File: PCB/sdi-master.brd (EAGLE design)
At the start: 71 x 18.2 mm, 21 parts, among them U1 ATSAMD11C14A-SSUT, U3 LDL1117S12R

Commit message: removed buttons.. not needed
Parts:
- removed R3: 2k, SparkFun-Resistors:1206
- removed S1: MOMENTARY-SWITCH-SPST-SMD-6.0X3.5MM, SparkFun-Switches:TACTILE_SWITCH_SMD_6.0X3.5MM
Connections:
- removed net N$1: R3.2, S1.1, U1.1
- net 3.3V: no longer S1.2
- net GND: no longer R3.1
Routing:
- net N$1: track 63.9 -> 0.00 mm, vias 2 -> 0
- net 3.3V: track 72.3 -> 60.1 mm
- net GND: vias 5 -> 1
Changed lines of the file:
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@@
 <?xml version="1.0" encoding="utf-8"?>
 <!DOCTYPE eagle SYSTEM "eagle.dtd">
-<eagle version="9.2.2">
+<eagle version="9.3.0">
 <drawing>
 <settings>
@@
 <attribute name="VALUE" x="31.67" y="14.032" size="0.6096" layer="27" font="vector" ratio="20" rot="R180"/>
 </element>
-<element name="S1" library="SparkFun-Switches" package="TACTILE_SWITCH_SMD_6.0X3.5MM" value="MOMENTARY-SWITCH-SPST-SMD-6.0X3.5MM" x="58.5" y="18.1" smashed="yes" rot="R270">
-<attribute name="NAME" x="60.405" y="18.1" size="0.6096" layer="25" font="vector" ratio="20" rot="R270" align="bottom-center"/>
-<attribute name="PROD_ID" value="SWCH-00815" x="58.5" y="18.1" size="1.778" layer="27" rot="R270" display="off"/>
-<attribute name="SF_SKU" value="COM-08229" x="58.5" y="18.1" size="1.778" layer="27" rot="R270" display="off"/>
-</element>
-<element name="R3" library="SparkFun-Resistors" package="1206" value="2k" x="54.6" y="13.1" smashed="yes">
-<attribute name="NAME" x="53.33" y="14.243" size="0.4064" layer="25"/>
-<attribute name="VALUE" x="53.203" y="11.576" size="0.4064" layer="27"/>
-</element>
 </elements>
 <signals>
@@
 <contactref element="J1" pad="SHIELD3"/>
 <contactref element="J2" pad="1"/>
-<contactref element="R3" pad="1"/>
-<via x="47.6" y="17.2" extent="1-16" drill="0.25"/>
-<via x="53.8" y="16.7" extent="1-16" drill="0.25"/>
-<via x="52.1" y="14.9" extent="1-16" drill="0.25"/>
-<via x="47.2" y="14.9" extent="1-16" drill="0.25"/>
 <wire x1="37.69" y1="12.847" x2="36.937" y2="13.6" width="0.254" layer="1"/>
 <wire x1="36.937" y1="13.6" x2="36.3" y2="13.6" width="0.254" layer="1"/>
@@
 <wire x1="36.3" y1="13.6" x2="34.7" y2="12" width="0.254" layer="16"/>
 <wire x1="34.7" y1="12" x2="30.4" y2="12" width="0.254" layer="16"/>
+<wire x1="50.502" y1="22.646" x2="53.15" y2="20" width="0" layer="19" extent="1-1"/>
+<wire x1="47.85" y1="20" x2="50.502" y2="22.646" width="0" layer="19" extent="1-1"/>
+<wire x1="50.502" y1="17.346" x2="53.15" y2="20" width="0" layer="19" extent="1-1"/>
+<wire x1="44.724" y1="17.904" x2="47.85" y2="20" width="0" layer="19" extent="1-1"/>
+<wire x1="50.412" y1="13.325" x2="50.502" y2="17.346" width="0" layer="19" extent="1-1"/>
+<wire x1="37.69" y1="12.847" x2="44.724" y2="17.904" width="0" layer="19" extent="1-1"/>
+<wire x1="12.31" y1="18.6452" x2="30.4" y2="12" width="0" layer="19" extent="1-1"/>
+<wire x1="9.2844" y1="21.1468" x2="12.31" y2="18.6452" width="0" layer="19" extent="1-1"/>
+<wire x1="1.957" y1="20.255" x2="9.2844" y2="21.1468" width="0" layer="19" extent="1-1"/>
+<wire x1="1.957" y1="16.57" x2="1.957" y2="20.255" width="0" layer="19" extent="1-1"/>
+<wire x1="4.682" y1="15.27" x2="1.957" y2="16.57" width="0" layer="19" extent="1-1"/>
+<wire x1="1.957" y1="12.885" x2="4.682" y2="15.27" width="0" layer="19" extent="1-1"/>
 </signal>
 <signal name="PWM">
@@
 <wire x1="46.791" y1="11.604" x2="48.512" y2="13.325" width="0.4064" layer="1"/>
 <wire x1="41.32" y1="10.5" x2="42.21" y2="11.39" width="0.254" layer="1"/>
-<contactref element="S1" pad="2"/>
 <wire x1="40" y1="10.5" x2="41.32" y2="10.5" width="0.254" layer="1"/>
-<wire x1="58.5" y1="14.95" x2="57.827" y2="14.277" width="0.254" layer="1"/>
-<wire x1="57.827" y1="14.277" x2="57.827" y2="12.6881875" width="0.254" layer="1"/>
-<wire x1="57.827" y1="12.6881875" x2="56.3388125" y2="11.2" width="0.254" layer="1"/>
-<wire x1="49.381" y1="12.4171875" x2="49.381" y2="12.456" width="0.254" layer="1"/>
-<wire x1="49.381" y1="12.456" x2="48.512" y2="13.325" width="0.254" layer="1"/>
-<wire x1="50.5981875" y1="11.2" x2="49.381" y2="12.4171875" width="0.254" layer="1"/>
-<wire x1="56.3388125" y1="11.2" x2="50.5981875" y2="11.2" width="0.254" layer="1"/>
 <wire x1="21.68256875" y1="15.0168" x2="23.6708625" y2="15.0168" width="0.4064" layer="1"/>
 <wire x1="25.71725" y1="14.14275" x2="27.86" y2="12" width="0.4064" layer="1"/>
@@
 <wire x1="11.04" y1="20.3" x2="10.9844" y2="20.3556" width="0.4064" layer="1"/>
 <wire x1="10.9844" y1="20.3556" x2="10.9844" y2="21.1468" width="0.4064" layer="1"/>
-<wire x1="42.424" y1="11.604" x2="42.424" y2="13.924" width="0.4064" layer="1"/>
-<wire x1="42.424" y1="13.924" x2="42.5" y2="14" width="0.4064" layer="1"/>
-<via x="42.5" y="14" extent="1-16" drill="0.3937"/>
-<wire x1="42.5" y1="14" x2="42.5" y2="15.2" width="0.4064" layer="16"/>
-<wire x1="42.5" y1="15.2" x2="41.6" y2="16.1" width="0.4064" layer="16"/>
-<via x="41.6" y="16.1" extent="1-16" drill="0.3937"/>
-<wire x1="41.6" y1="16.1" x2="42.424" y2="16.924" width="0.4064" layer="1"/>
-<wire x1="42.424" y1="16.924" x2="42.424" y2="17.904" width="0.4064" layer="1"/>
+<wire x1="42.424" y1="11.604" x2="42.424" y2="12.624" width="0.4064" layer="1"/>
+<wire x1="42.424" y1="12.624" x2="43.7" y2="13.9" width="0.4064" layer="1"/>
+<via x="43.7" y="13.9" extent="1-16" drill="0.3937"/>
+<wire x1="43.7" y1="13.9" x2="41.4" y2="16.2" width="0.4064" layer="16"/>
+<via x="41.4" y="16.2" extent="1-16" drill="0.3937"/>
+<wire x1="41.4" y1="16.2" x2="42.424" y2="17.224" width="0.4064" layer="1"/>
+<wire x1="42.424" y1="17.224" x2="42.424" y2="17.904" width="0.4064" layer="1"/>
 </signal>
 <signal name="SWDIO">
@@
 <wire x1="14.85" y1="13.05" x2="14.85" y2="13.7452" width="0.2032" layer="1"/>
 </signal>
-<signal name="N$1">
-<contactref element="S1" pad="1"/>
-<contactref element="R3" pad="2"/>
-<contactref element="U1" pad="1"/>
-<wire x1="56" y1="13.1" x2="57.319" y2="14.419" width="0.254" layer="1"/>
-<wire x1="57.319" y1="14.419" x2="57.319" y2="16.2578125" width="0.254" layer="1"/>
-<wire x1="58" y1="16.9388125" x2="58" y2="20.9" width="0.254" layer="1"/>
-<wire x1="56.8069875" y1="15.7458" x2="57.319" y2="16.2578125" width="0.254" layer="1"/>
-<wire x1="57.319" y1="16.2578125" x2="58" y2="16.9388125" width="0.254" layer="1"/>
-<wire x1="58" y1="20.9" x2="58.15" y2="20.9" width="0.254" layer="1"/>
-<wire x1="58.15" y1="20.9" x2="58.5" y2="21.25" width="0.254" layer="1"/>
-<via x="27.8" y="13.9" extent="1-16" drill="0.3937"/>
-<wire x1="56.8069875" y1="15.7458" x2="42.805775" y2="15.7458" width="0.254" layer="1"/>
-<wire x1="38.726775" y1="11.6668" x2="36.953225" y2="11.6668" width="0.254" layer="1"/>
-<wire x1="36.953225" y1="11.6668" x2="34.720025" y2="13.9" width="0.254" layer="1"/>
-<wire x1="34.720025" y1="13.9" x2="27.8" y2="13.9" width="0.254" layer="1"/>
-<wire x1="42.805775" y1="15.7458" x2="38.726775" y2="11.6668" width="0.254" layer="1"/>
-<wire x1="27.8" y1="13.9" x2="13.9" y2="13.9" width="0.254" layer="16"/>
-<wire x1="13.9" y1="13.9" x2="11.7" y2="11.7" width="0.254" layer="16"/>
-<wire x1="11.7" y1="11.7" x2="8.5" y2="11.7" width="0.254" layer="16"/>
-<via x="8.5" y="11.7" extent="1-16" drill="0.3937"/>
-<wire x1="8.5" y1="11.7" x2="8.5" y2="13.7452" width="0.254" layer="1"/>
-</signal>
 </signals>

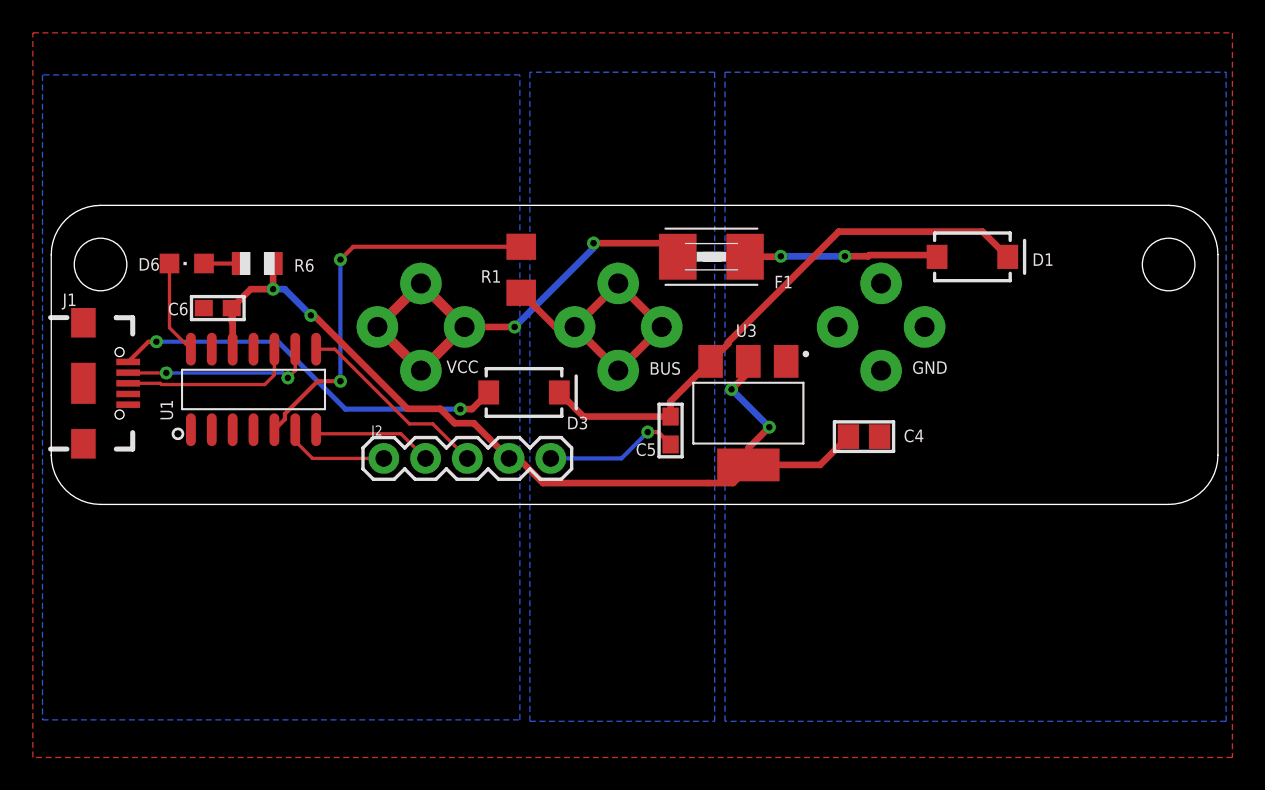
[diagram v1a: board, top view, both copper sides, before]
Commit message: added power connectors to sdi master
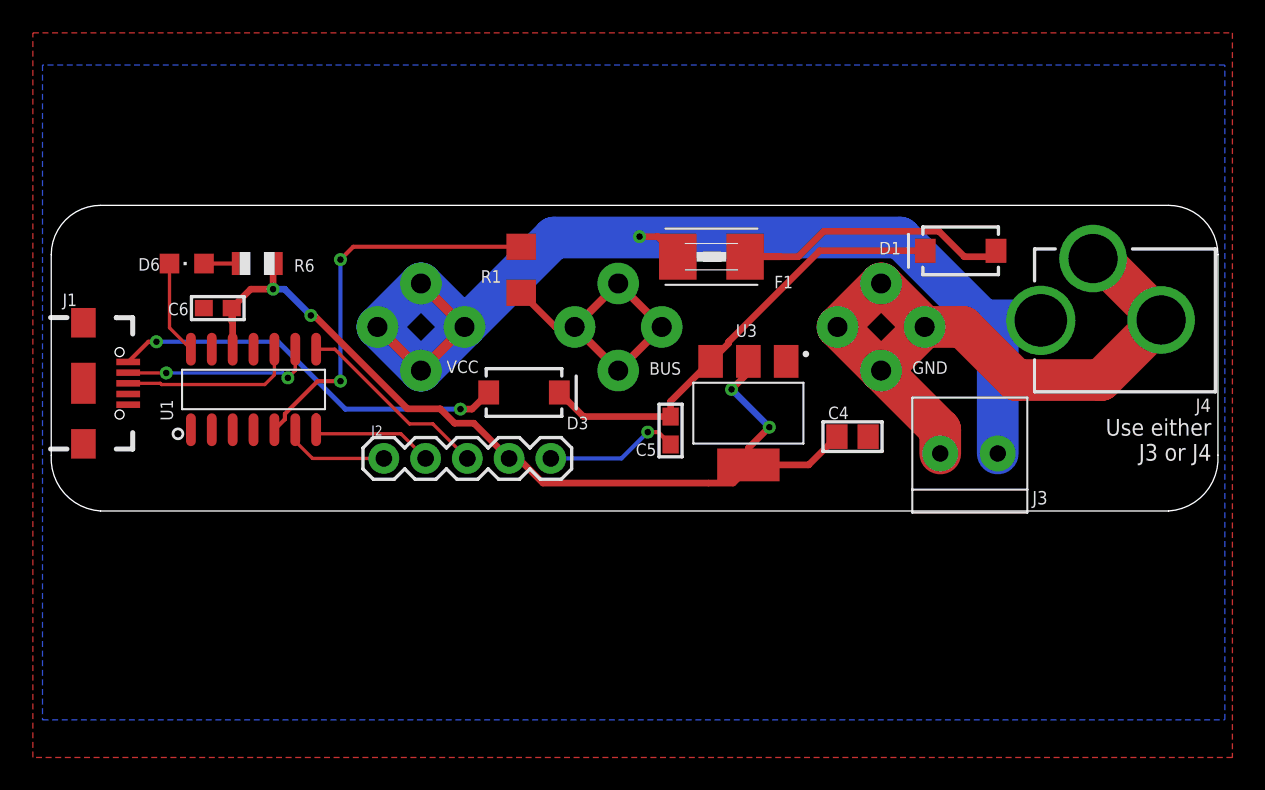
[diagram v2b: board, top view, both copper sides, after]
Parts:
- added J3: 1X2-3.5MM, Adafruit:1X2-3.5MM
- added J4: POWER_JACKPTH_LOCK, SparkFun-Connectors:POWER_JACK_PTH_LOCK
- moved D1 0.81 mm to (55.3, 24.6), turned to 180 degrees
- moved C4 0.70 mm to (48.8, 13.3)
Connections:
- net GND: now also J3.2, J4.GND, J4.GNDBREAK
- net VCC-RAW: now also J3.1, J4.PWR
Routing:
- net VCC-RAW: track 30.7 -> 77.3 mm, vias 2 -> 1
- net GND: track 8.26 -> 52.7 mm
- net N$12: track 11.8 -> 18.9 mm, vias 2 -> 0
- net VCC: track 33.8 -> 27.7 mm
- net 3.3V: track 60.1 -> 59.4 mm
- removed copper zone on layer 16, net BUS
- removed copper zone on layer 16, net GND
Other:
- board size 71 x 18.2 mm -> 71 x 18.6 mm
- board text added: "Use either J3 or J4"
